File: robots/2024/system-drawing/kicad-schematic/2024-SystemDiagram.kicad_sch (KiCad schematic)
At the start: 197 parts

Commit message: Change Note Retiontion to Note Hold
Signed-off-by: Scott Berman <sgberman1@gmail.com>
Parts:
- MOT15: value Kraken Note Retention -> Kraken Note Hold
- W18: value NOTE RETENTION PWR -> NOTE_HOLD_PWR
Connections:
- net at POE1. (RJ45S): now also RDO1. (POWER); no longer VRM1. (5V/2A)
- net at RDO1. (POWER): now also ETH1. (POWER); no longer VRM1. (5V/2A)
- net at ETH1. (POWER): now also NX1. (Power), W87.; no longer RDO1. (POWER)
- net CAN_CANDLE_TO_RETENTION renamed CAN_CANDLE_TO_HOLD
- removed net CAN_RETENTION_TO_ALT: MOT15. (PWR), MOT7. (PWR), W127.
- net NOTE RETENTION PWR renamed NOTE HOLD PWR
- new net: VRM1. (5V/2A), W118., WG1. (4)
- new net: POE1. (RJ45S), VRM1. (5V/2A)
- new net: RDO1. (POWER), VRM1. (5V/2A)
- new net: CAN1. (USB), W67., WG1. (4)
- new net: ETH1. (POWER), NX2. (Power), W88.
- new net: MOT10. (PWR), MOT12. (PWR), W111.
- new net: VRM2. (5V/2A), W85., WG101. (3)
- new net: ETH1. (POWER), VRM2. (5V/2A), W84.
- new net: ETH1. (POWER), NX3. (Power), W89.
- new net: PD2. (IN), WG101. (3)
- new net: MOT1. (PWR), MOT2. (PWR), W105.
- new net: MOT3. (PWR), MOT4. (PWR), W107.
- new net: IMU1. (RIO_PWM2), NX3. (Power), W47.
- new net CAN_HOLD_TO_ALT: MOT15. (PWR), MOT7. (PWR), W127.
- now unconnected: VRM2. (5V/2A), VRM2. (5V/2A)
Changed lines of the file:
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@@
     (effects (font (face "FreeSans") (size 1.27 1.27) bold) (justify left bottom))
   )
-  (label "CAN_CANDLE_TO_RETENTION" (at 581.66 459.74 180) (fields_autoplaced)
+  (label "CAN_CANDLE_TO_HOLD" (at 581.66 459.74 180) (fields_autoplaced)
     (effects (font (face "FreeSans") (size 1.27 1.27) bold) (justify right bottom))
   )
@@
     (effects (font (face "FreeSans") (size 1.27 1.27) bold) (justify left bottom))
   )
-  (label "CAN_RETENTION_TO_ALT" (at 581.66 454.66 180) (fields_autoplaced)
+  (label "CAN_HOLD_TO_ALT" (at 581.66 454.66 180) (fields_autoplaced)
     (effects (font (face "FreeSans") (size 1.27 1.27) bold) (justify right bottom))
   )
@@
     (effects (font (face "FreeSans") (size 1.27 1.27) bold) (justify left bottom))
   )
-  (label "NOTE RETENTION PWR" (at 242.57 113.03 0) (fields_autoplaced)
+  (label "NOTE HOLD PWR" (at 242.57 113.03 0) (fields_autoplaced)
     (effects (font (face "FreeSans") (size 1.27 1.27) bold) (justify left bottom))
   )
@@
     (effects (font (face "FreeSans") (size 1.27 1.27) bold) (justify left bottom))
   )
-  (label "CAN_CANDLE_TO_RETENTION" (at 557.53 474.98 180) (fields_autoplaced)
+  (label "CAN_CANDLE_TO_HOLD" (at 557.53 474.98 180) (fields_autoplaced)
     (effects (font (face "FreeSans") (size 1.27 1.27) bold) (justify right bottom))
   )
@@
     (effects (font (face "FreeSans") (size 1.27 1.27) bold) (justify left bottom))
   )
-  (label "CAN_RETENTION_TO_ALT" (at 586.74 198.12 180) (fields_autoplaced)
+  (label "CAN_HOLD_TO_ALT" (at 586.74 198.12 180) (fields_autoplaced)
     (effects (font (face "FreeSans") (size 1.27 1.27) bold) (justify right bottom))
   )
@@
       (effects (font (face "FreeSans") (size 1.524 1.524) bold) (justify left))
     )
-    (property "Value" "Kraken Note Retention" (at 623.57 455.93 0)
+    (property "Value" "Kraken Note Hold" (at 623.57 455.93 0)
       (effects (font (face "FreeSans") (size 1.524 1.524) bold) (justify left))
     )
@@
       (effects (font (face "FreeSans") (size 1.524 1.524) bold))
     )
-    (property "Value" "NOTE RETENTION PWR" (at 487.68 449.58 0)
+    (property "Value" "NOTE_HOLD_PWR" (at 487.68 449.58 0)
       (effects (font (face "FreeSans") (size 1.524 1.524) bold))
     )

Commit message: Updating system diagram to reflect the robot wiring
Signed-off-by: Scott Berman <sgberman1@gmail.com>
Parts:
- removed POT3: Intake Pivot Pot, symbol SystemDiagram:Pot
- removed W29: Intake Pivot Pot, symbol SystemDiagram:WireTag
- added WJ101, WJ102, WJ103, WJ104, WJ105, WJ106, WJ107, WJ108, WJ109, WJ110, WJ111, WJ113: ~, symbol SystemDiagram:Wire_Junction
- BB2: value Catapult BeamBreakSensor -> Shooter BeamBreakSensor
- W24: value Catapult Beam Break -> Shooter Beam Break
- W54: value TEMP BEAM BREAK RIO -> SHOOTER BEAM BREAK RIO
- W63: value TEMP BB PWR -> Shooter BB PWR
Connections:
- net CAN_ALT_TO_XFER_ROLLERS: now also WJ108.1 (J)
- net CAN_CANDLE_TO_HOLD: now also WJ111.1 (J); no longer W115.
- net CAN_EXTEND_TO_DUMP: now also WJ110.1 (J)
- net CAN_INTAKE_TO_CANDLE: now also W115., WJ109.1 (J), WJ113.1 (J)
- net CAT ALTITUDE ENC POT RIO: now also WJ107.1 (J)
- net CAT ENC POT RIO: now also WJ105.1 (J)
- net CATAPULT ALTITUDE PWR: now also WJ106.1 (J)
- net CATAPULT1 PWM: now also WJ102.1 (J)
- net CATAPULT1 PWR: now also WJ101.1 (J)
- net CATAPULT2 PWM: now also WJ104.1 (J)
- net CATAPULT2 PWR: now also WJ103.1 (J)
- net at POE1. (RJ45S): now also RDO1. (POWER); no longer VRM1. (5V/2A)
- net at RDO1. (POWER): now also ETH1. (POWER); no longer VRM1. (5V/2A)
- net at ETH1. (POWER): now also NX1. (Power), W87.; no longer RDO1. (POWER)
- removed net CAT BB PWR: BBA2. (SNSR), W63., WG1. (4)
- net TEMP BEAM BREAK renamed SHOOTER BEAM BREAK
- new net: VRM1. (5V/2A), W118., WG1. (4)
- new net: POE1. (RJ45S), VRM1. (5V/2A)
- new net: RDO1. (POWER), VRM1. (5V/2A)
- new net: CAN1. (USB), W67., WG1. (4)
- new net: ETH1. (POWER), NX2. (Power), W88.
- new net: MOT10. (PWR), MOT12. (PWR), W111.
- new net: VRM2. (5V/2A), W85., WG101. (3)
- new net: ETH1. (POWER), VRM2. (5V/2A), W84.
- new net: ETH1. (POWER), NX3. (Power), W89.
- new net: PD2. (IN), WG101. (3)
- new net: MOT1. (PWR), MOT2. (PWR), W105.
- new net: MOT3. (PWR), MOT4. (PWR), W107.
- new net: IMU1. (RIO_PWM2), NX3. (Power), W47.
- new net SHOOTER BB PWR: BBA2. (SNSR), W63., WG1. (4)
- now unconnected: VRM2. (5V/2A), VRM2. (5V/2A)
- no-connect marks 72 -> 73
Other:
- moved on the sheet: BB2, BBA2, MAG1, MGA6, MOT7, POT1, W10, W108, W117, W125, W126, W128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

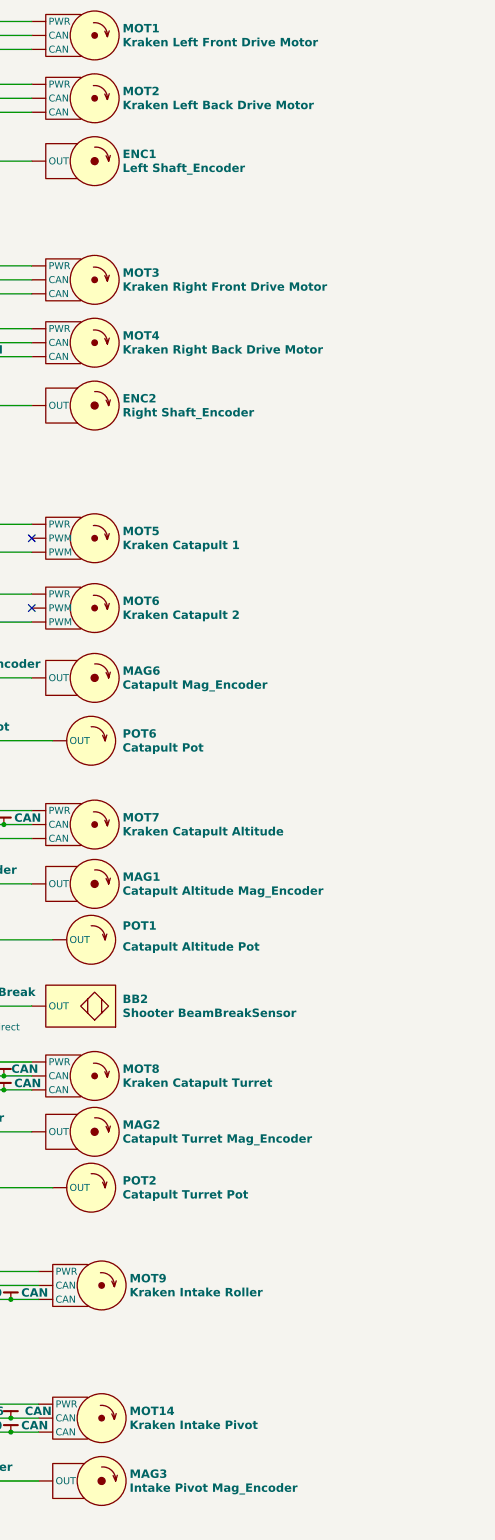
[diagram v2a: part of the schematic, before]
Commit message: Adding CAN FD IDs to sys drawing
Signed-off-by: Scott Berman <sgberman1@gmail.com>
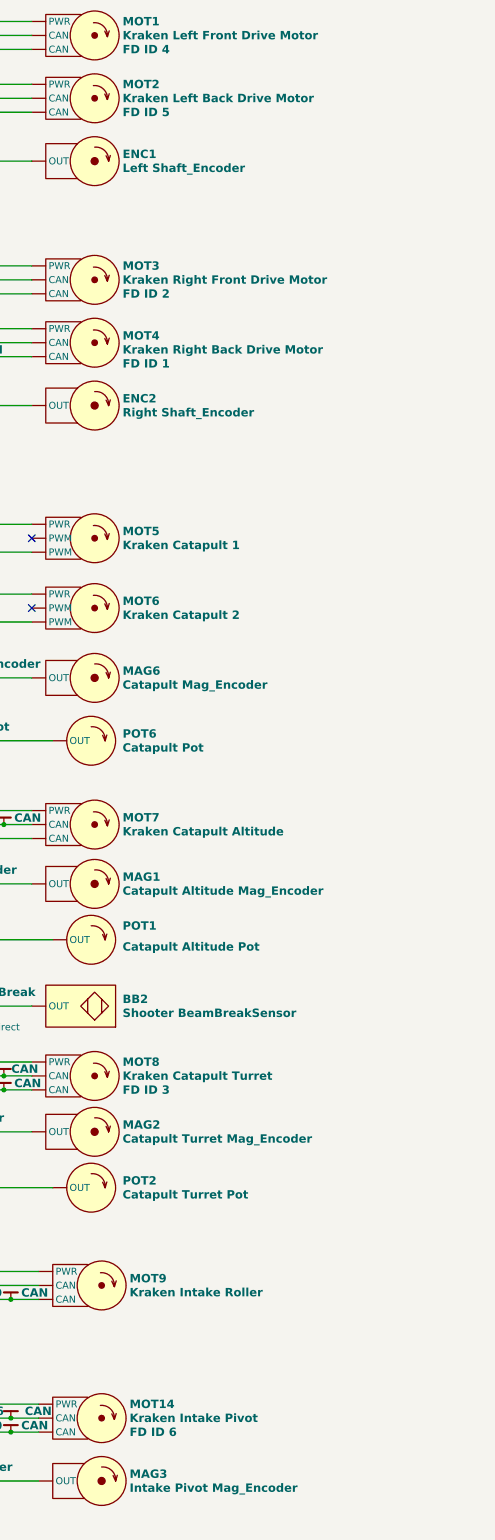
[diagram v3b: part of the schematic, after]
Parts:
- MOT1: CAN ID (none) -> FD ID 4
- MOT14: CAN ID (none) -> FD ID 6
- MOT2: CAN ID (none) -> FD ID 5
- MOT3: CAN ID (none) -> FD ID 2
- MOT4: CAN ID (none) -> FD ID 1
- MOT8: CAN ID (none) -> FD ID 3
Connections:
- net at POE1. (RJ45S): now also RDO1. (POWER); no longer VRM1. (5V/2A)
- net at RDO1. (POWER): now also ETH1. (POWER); no longer VRM1. (5V/2A)
- net at ETH1. (POWER): now also NX1. (Power), W87.; no longer RDO1. (POWER)
- new net: VRM1. (5V/2A), W118., WG1. (4)
- new net: POE1. (RJ45S), VRM1. (5V/2A)
- new net: RDO1. (POWER), VRM1. (5V/2A)
- new net: CAN1. (USB), W67., WG1. (4)
- new net: ETH1. (POWER), NX2. (Power), W88.
- new net: MOT10. (PWR), MOT12. (PWR), W111.
- new net: VRM2. (5V/2A), W85., WG101. (3)
- new net: ETH1. (POWER), VRM2. (5V/2A), W84.
- new net: ETH1. (POWER), NX3. (Power), W89.
- new net: PD2. (IN), WG101. (3)
- new net: MOT1. (PWR), MOT2. (PWR), W105.
- new net: MOT3. (PWR), MOT4. (PWR), W107.
- new net: IMU1. (RIO_PWM2), NX3. (Power), W47.
- now unconnected: VRM2. (5V/2A), VRM2. (5V/2A)
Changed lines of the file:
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@@
     )
   )
-  (symbol (lib_id "SystemDiagram:Falcon_Motor") (at 608.33 227.33 0) (unit 1)
+  (symbol (lib_name "Falcon_Motor_4") (lib_id "SystemDiagram:Falcon_Motor") (at 608.33 227.33 0) (unit 1)
     (in_bom yes) (on_board yes) (dnp no) (fields_autoplaced)
-    (property "Reference" "MOT8" (at 622.3 226.06 0)
+    (property "Reference" "MOT8" (at 622.3 224.79 0)
       (effects (font (face "FreeSans") (size 1.524 1.524) bold) (justify left))
     )
-    (property "Value" "Kraken Catapult Turret" (at 622.3 228.6 0)
+    (property "Value" "Kraken Catapult Turret" (at 622.3 227.33 0)
       (effects (font (face "FreeSans") (size 1.524 1.524) bold) (justify left))
     )
@@
       (effects (font (size 1.27 1.27)) hide)
     )
+    (property "CAN ID" "FD ID 3" (at 622.3 229.87 0)
+      (effects (font (face "FreeSans") (size 1.524 1.524) bold) (justify left))
+    )
     (pin "")
     (pin "")
@@
     )
   )
-  (symbol (lib_id "SystemDiagram:Falcon_Motor") (at 608.33 49.53 0) (unit 1)
+  (symbol (lib_name "Falcon_Motor_7") (lib_id "SystemDiagram:Falcon_Motor") (at 608.33 49.53 0) (unit 1)
     (in_bom yes) (on_board yes) (dnp no) (fields_autoplaced)
-    (property "Reference" "MOT2" (at 622.3 48.26 0)
+    (property "Reference" "MOT2" (at 622.3 46.99 0)
       (effects (font (face "FreeSans") (size 1.524 1.524) bold) (justify left))
     )
-    (property "Value" "Kraken Left Back Drive Motor" (at 622.3 50.8 0)
+    (property "Value" "Kraken Left Back Drive Motor" (at 622.3 49.53 0)
       (effects (font (face "FreeSans") (size 1.524 1.524) bold) (justify left))
     )
@@
       (effects (font (size 1.27 1.27)) hide)
     )
+    (property "CAN ID" "FD ID 5" (at 622.3 52.07 0)
+      (effects (font (face "FreeSans") (size 1.524 1.524) bold) (justify left))
+    )
     (pin "")
     (pin "")
@@
     )
   )
-  (symbol (lib_id "SystemDiagram:Falcon_Motor") (at 608.33 38.1 0) (unit 1)
+  (symbol (lib_name "Falcon_Motor_6") (lib_id "SystemDiagram:Falcon_Motor") (at 608.33 38.1 0) (unit 1)
     (in_bom yes) (on_board yes) (dnp no) (fields_autoplaced)
-    (property "Reference" "MOT1" (at 622.3 36.83 0)
+    (property "Reference" "MOT1" (at 622.3 35.56 0)
       (effects (font (face "FreeSans") (size 1.524 1.524) bold) (justify left))
     )
-    (property "Value" "Kraken Left Front Drive Motor" (at 622.3 39.37 0)
+    (property "Value" "Kraken Left Front Drive Motor" (at 622.3 38.1 0)
       (effects (font (face "FreeSans") (size 1.524 1.524) bold) (justify left))
     )
@@
       (effects (font (size 1.27 1.27)) hide)
     )
+    (property "CAN ID" "FD ID 4" (at 622.3 40.64 0)
+      (effects (font (face "FreeSans") (size 1.524 1.524) bold) (justify left))
+    )
     (pin "")
     (pin "")
@@
       (effects (font (size 1.27 1.27)) hide)
     )
+    (property "CAN ID" "" (at 609.6 265.43 0)
+      (effects (font (size 1.27 1.27)))
+    )
     (pin "")
     (pin "")
@@
     )
   )
-  (symbol (lib_id "SystemDiagram:Falcon_Motor") (at 609.6 289.56 0) (unit 1)
+  (symbol (lib_name "Falcon_Motor_3") (lib_id "SystemDiagram:Falcon_Motor") (at 609.6 289.56 0) (unit 1)
     (in_bom yes) (on_board yes) (dnp no) (fields_autoplaced)
-    (property "Reference" "MOT14" (at 623.57 288.29 0)
+    (property "Reference" "MOT14" (at 623.57 287.02 0)
       (effects (font (face "FreeSans") (size 1.524 1.524) bold) (justify left))
     )
-    (property "Value" "Kraken Intake Pivot" (at 623.57 290.83 0)
+    (property "Value" "Kraken Intake Pivot" (at 623.57 289.56 0)
       (effects (font (face "FreeSans") (size 1.524 1.524) bold) (justify left))
     )
@@
       (effects (font (size 1.27 1.27)) hide)
     )
+    (property "CAN ID" "FD ID 6" (at 623.57 292.1 0)
+      (effects (font (face "FreeSans") (size 1.524 1.524) bold) (justify left))
+    )
     (pin "")
     (pin "")
@@
   )
   (symbol (lib_id "SystemDiagram:Falcon_Motor") (at 608.33 93.98 0) (unit 1)
-    (in_bom yes) (on_board yes) (dnp no) (fields_autoplaced)
+    (in_bom yes) (on_board yes) (dnp no)
     (property "Reference" "MOT4" (at 622.3 92.71 0)
       (effects (font (face "FreeSans") (size 1.524 1.524) bold) (justify left))
@@
       (effects (font (size 1.27 1.27)) hide)
     )
+    (property "CAN ID" "FD ID 1" (at 622.3 97.79 0)
+      (effects (font (face "FreeSans") (size 1.524 1.524) bold) (justify left))
+    )
     (pin "")
     (pin "")
@@
     )
   )
-  (symbol (lib_id "SystemDiagram:Falcon_Motor") (at 608.33 82.55 0) (unit 1)
+  (symbol (lib_name "Falcon_Motor_5") (lib_id "SystemDiagram:Falcon_Motor") (at 608.33 82.55 0) (unit 1)
     (in_bom yes) (on_board yes) (dnp no) (fields_autoplaced)
-    (property "Reference" "MOT3" (at 622.3 81.28 0)
+    (property "Reference" "MOT3" (at 622.3 80.01 0)
       (effects (font (face "FreeSans") (size 1.524 1.524) bold) (justify left))
     )
-    (property "Value" "Kraken Right Front Drive Motor" (at 622.3 83.82 0)
+    (property "Value" "Kraken Right Front Drive Motor" (at 622.3 82.55 0)
       (effects (font (face "FreeSans") (size 1.524 1.524) bold) (justify left))
     )
@@
       (effects (font (size 1.27 1.27)) hide)
     )
+    (property "CAN ID" "FD ID 2" (at 622.3 85.09 0)
+      (effects (font (face "FreeSans") (size 1.524 1.524) bold) (justify left))
+    )
     (pin "")
